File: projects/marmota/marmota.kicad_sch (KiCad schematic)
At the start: 56 parts, among them J1 USB_C, J2 Conn_01x20_Pin, J3 Conn_01x20_Pin, SW1 Button top, SW2 Button side, U1 RP2040, U2 FLASH, U3 MCP73871, U4 RT6160, U5 ESP32, Y1 12MHz

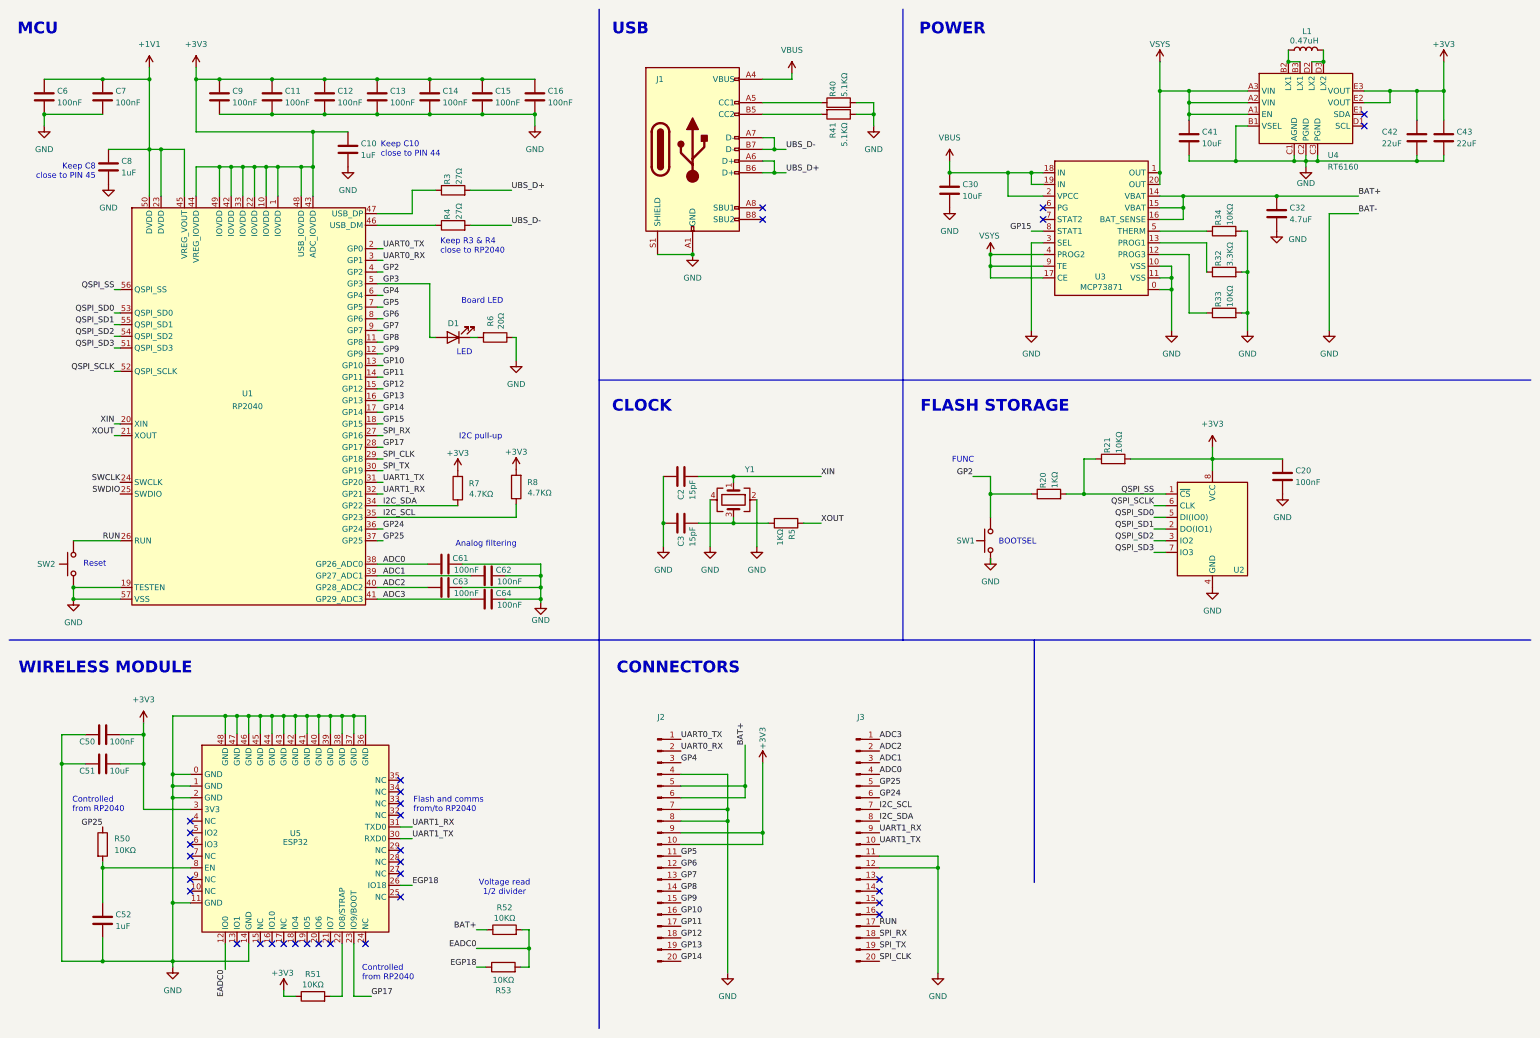
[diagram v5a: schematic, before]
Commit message: Changed power output caps to 47uF in 0603 footprint
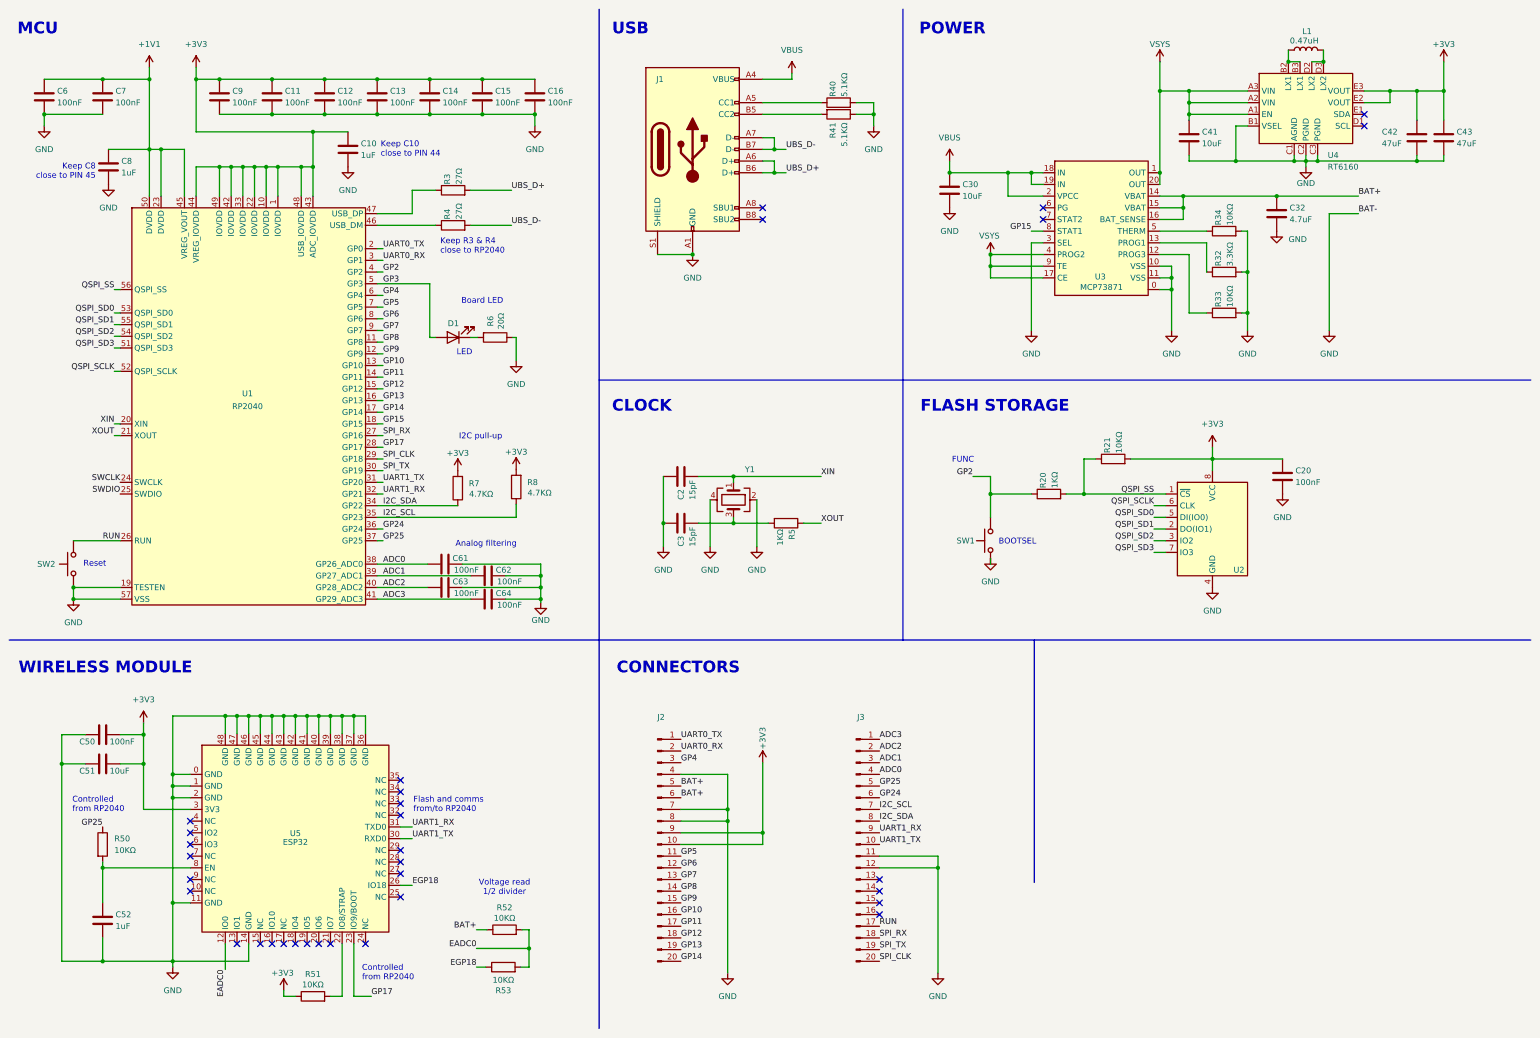
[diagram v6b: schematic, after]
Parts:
- C42, C43: value 22uF -> 47uF; footprint ILO_fp:0402_compact -> ILO_fp:0603_compact; LCSC C105226 -> C730416
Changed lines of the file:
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@@
 	)
 	(junction
-		(at 172.72 181.61)
-		(diameter 0)
-		(color 0 0 0 0)
-	)
-	(junction
 		(at 81.28 27.94)
 		(diameter 0)
@@
 	(wire
 		(pts
-			(xy 172.72 184.15) (xy 172.72 181.61)
-		)
-		(stroke
-			(width 0)
-			(type default)
-		)
-	)
-	(wire
-		(pts
 			(xy 80.01 166.37) (xy 80.01 170.18)
 		)
@@
 	(wire
 		(pts
-			(xy 172.72 181.61) (xy 172.72 172.72)
-		)
-		(stroke
-			(width 0)
-			(type default)
-		)
-	)
-	(wire
-		(pts
 			(xy 93.98 105.41) (xy 92.71 105.41)
 		)
@@
 	(wire
 		(pts
-			(xy 158.75 181.61) (xy 172.72 181.61)
-		)
-		(stroke
-			(width 0)
-			(type default)
-		)
-	)
-	(wire
-		(pts
 			(xy 24.13 176.784) (xy 24.13 219.71)
 		)
@@
 	(wire
 		(pts
-			(xy 158.75 184.15) (xy 172.72 184.15)
-		)
-		(stroke
-			(width 0)
-			(type default)
-		)
-	)
-	(wire
-		(pts
 			(xy 256.54 110.49) (xy 274.32 110.49)
 		)
@@
 		)
 	)
+	(label "BAT+"
+		(at 158.75 184.15 0)
+		(fields_autoplaced yes)
+		(effects
+			(font
+				(size 1.27 1.27)
+			)
+			(justify left bottom)
+		)
+	)
 	(label "ADC2"
 		(at 93.98 138.43 0)
@@
 	)
 	(label "BAT+"
-		(at 172.72 172.72 90)
+		(at 158.75 181.61 0)
 		(fields_autoplaced yes)
 		(effects
@@
 			)
 		)
-		(property "Value" "22uF"
+		(property "Value" "47uF"
 			(at 311.15 41.91 0)
 			(effects
@@
 			)
 		)
-		(property "Footprint" "ILO_fp:0402_compact"
+		(property "Footprint" "ILO_fp:0603_compact"
 			(at 317.8048 36.83 0)
 			(effects
@@
 			)
 		)
-		(property "LCSC" "C105226"
+		(property "LCSC" "C730416"
 			(at 318.77 40.64 0)
 			(effects
@@
 			)
 		)
-		(property "Value" "22uF"
+		(property "Value" "47uF"
 			(at 327.406 41.91 0)
 			(effects
@@
 			)
 		)
-		(property "Footprint" "ILO_fp:0402_compact"
+		(property "Footprint" "ILO_fp:0603_compact"
 			(at 323.6468 36.83 0)
 			(effects
@@
 			)
 		)
-		(property "LCSC" "C105226"
+		(property "LCSC" "C730416"
 			(at 324.612 40.64 0)
 			(effects

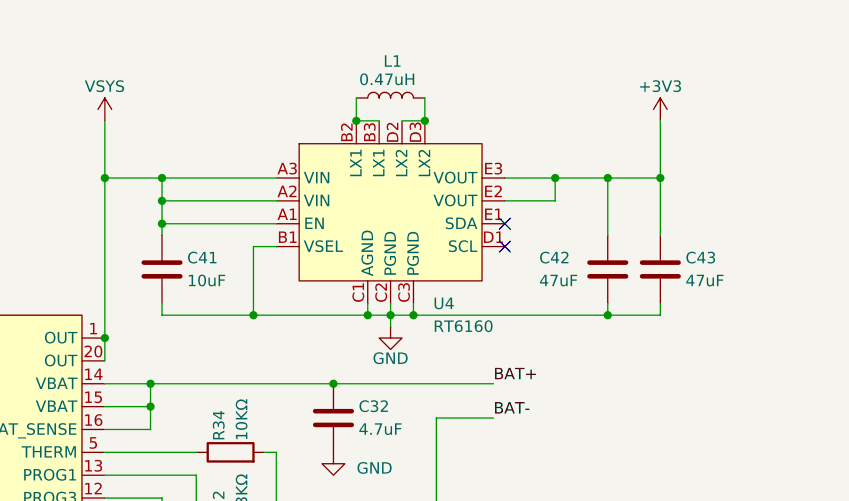
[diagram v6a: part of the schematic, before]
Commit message: Using Richtek 6150 instead of 6160
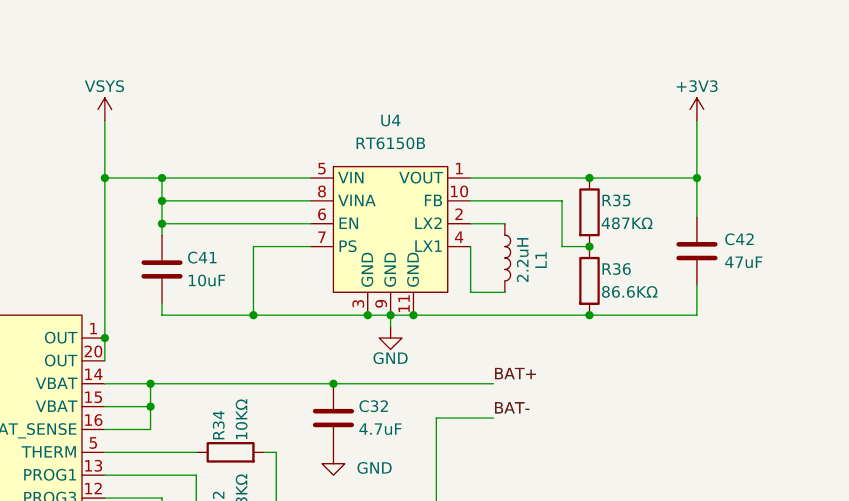
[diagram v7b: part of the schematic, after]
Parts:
- removed C43: 47uF, ILO_fp:0603_compact, symbol Device:C
- removed U4: RT6160, ILO_fp:WL-CSP-15B-1.4x2.3, symbol ILO_sym:Richtek_RT6160
- added R35: 487KΩ, ILO_fp:0402_compact, symbol Device:R
- added R36: 86.6KΩ, ILO_fp:0402_compact, symbol Device:R
- added U4: RT6150B, ILO_fp:WDFN-10L-2.5x2.5, symbol ILO_sym:Richtek_RT6150
- L1: value 0.47uH -> 2.2uH; footprint ILO_fp:SMD_16x10 -> ILO_fp:0603_compact; LCSC C5832340 -> C394950
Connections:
- net +3V3: now also R35.1, U4.1 (VOUT)
- net GND: now also R36.2, U4.11 (GND), U4.3 (GND), U4.7 (PS), U4.9 (GND)
- net VSYS: now also U4.5 (VIN), U4.6 (EN), U4.8 (VINA)
- net at L1.1: now also U4.2 (LX2)
- net at L1.2: now also U4.4 (LX1)
- new net: R35.2, R36.1, U4.10 (FB)
- no-connect marks 33 -> 31
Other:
- moved on the sheet: C42, L1

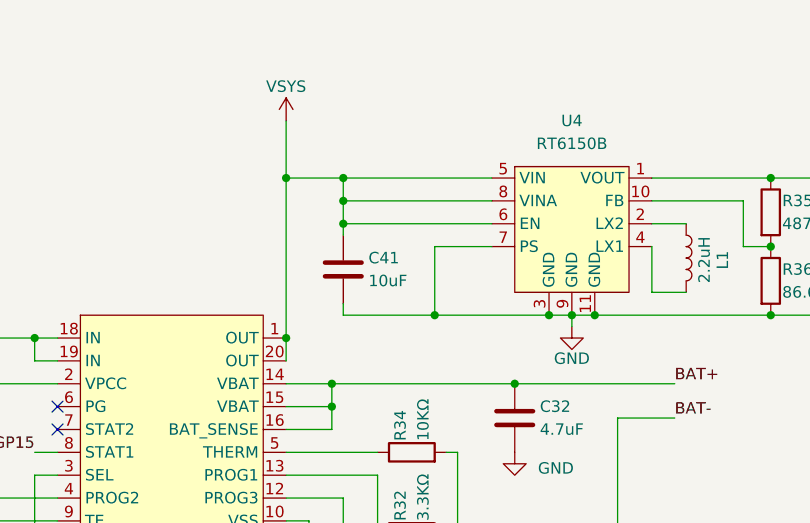
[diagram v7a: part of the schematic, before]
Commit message: Richtek power saving high, Tweaks
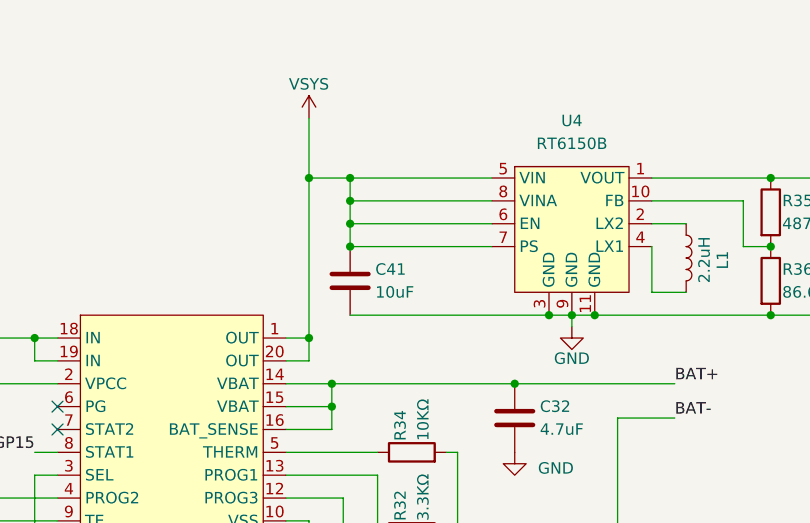
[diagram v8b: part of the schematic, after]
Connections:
- net GND: no longer U4.7 (PS)
- net VSYS: now also U4.7 (PS)
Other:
- moved on the sheet: C41
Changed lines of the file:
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@@
 	)
 	(junction
-		(at 269.24 35.56)
+		(at 270.002 35.56)
 		(diameter 0)
 		(color 0 0 0 0)
@@
 	)
 	(junction
-		(at 269.24 33.02)
+		(at 270.002 33.02)
 		(diameter 0)
 		(color 0 0 0 0)
@@
 	)
 	(junction
-		(at 176.53 191.77)
+		(at 265.43 48.26)
 		(diameter 0)
 		(color 0 0 0 0)
 	)
 	(junction
-		(at 262.89 30.48)
+		(at 176.53 191.77)
 		(diameter 0)
 		(color 0 0 0 0)
@@
 	)
 	(junction
-		(at 279.4 45.72)
-		(diameter 0)
-		(color 0 0 0 0)
-	)
-	(junction
 		(at 78.74 46.99)
 		(diameter 0)
@@
 	)
 	(junction
-		(at 269.24 30.48)
+		(at 270.002 38.1)
+		(diameter 0)
+		(color 0 0 0 0)
+	)
+	(junction
+		(at 270.002 30.48)
 		(diameter 0)
 		(color 0 0 0 0)
@@
 	)
 	(junction
-		(at 262.89 48.26)
-		(diameter 0)
-		(color 0 0 0 0)
-	)
-	(junction
 		(at 297.18 45.72)
 		(diameter 0)
@@
 		(color 0 0 0 0)
 	)
+	(junction
+		(at 265.43 30.48)
+		(diameter 0)
+		(color 0 0 0 0)
+	)
 	(no_connect
 		(at 80.01 215.9)
@@
 	(wire
 		(pts
-			(xy 262.89 48.26) (xy 262.89 50.8)
-		)
-		(stroke
-			(width 0)
-			(type default)
-		)
-	)
-	(wire
-		(pts
 			(xy 45.72 43.18) (xy 45.72 53.34)
 		)
@@
 	(wire
 		(pts
-			(xy 269.24 30.48) (xy 285.75 30.48)
+			(xy 270.002 30.48) (xy 285.75 30.48)
 		)
 		(stroke
@@
 	(wire
 		(pts
-			(xy 269.24 45.72) (xy 279.4 45.72)
-		)
-		(stroke
-			(width 0)
-			(type default)
-		)
-	)
-	(wire
-		(pts
 			(xy 189.23 114.3) (xy 170.18 114.3)
 		)
@@
 	(wire
 		(pts
-			(xy 269.24 35.56) (xy 269.24 36.83)
+			(xy 270.002 35.56) (xy 270.002 38.1)
 		)
 		(stroke
@@
 	(wire
 		(pts
-			(xy 279.4 45.72) (xy 292.1 45.72)
+			(xy 270.002 45.72) (xy 292.1 45.72)
 		)
 		(stroke
@@
 	(wire
 		(pts
-			(xy 262.89 30.48) (xy 269.24 30.48)
+			(xy 265.43 30.48) (xy 270.002 30.48)
 		)
 		(stroke
@@
 	(wire
 		(pts
-			(xy 269.24 30.48) (xy 269.24 33.02)
+			(xy 270.002 30.48) (xy 270.002 33.02)
 		)
 		(stroke
@@
 	(wire
 		(pts
-			(xy 262.89 24.13) (xy 262.89 30.48)
-		)
-		(stroke
-			(width 0)
-			(type default)
-		)
-	)
-	(wire
-		(pts
 			(xy 226.06 71.12) (xy 237.49 71.12)
 		)
@@
 	(wire
 		(pts
-			(xy 279.4 38.1) (xy 285.75 38.1)
-		)
-		(stroke
-			(width 0)
-			(type default)
-		)
-	)
-	(wire
-		(pts
 			(xy 175.26 119.38) (xy 175.26 129.54)
 		)
@@
 	(wire
 		(pts
-			(xy 262.89 30.48) (xy 262.89 48.26)
+			(xy 265.43 23.876) (xy 265.43 30.48)
 		)
 		(stroke
@@
 	(wire
 		(pts
+			(xy 265.43 48.26) (xy 262.89 48.26)
+		)
+		(stroke
+			(width 0)
+			(type default)
+		)
+	)
+	(wire
+		(pts
 			(xy 288.29 53.34) (xy 306.07 53.34)
 		)
@@
 	(wire
 		(pts
-			(xy 269.24 33.02) (xy 269.24 35.56)
+			(xy 270.002 33.02) (xy 270.002 35.56)
 		)
 		(stroke
@@
 	(wire
 		(pts
-			(xy 269.24 33.02) (xy 285.75 33.02)
+			(xy 270.002 33.02) (xy 285.75 33.02)
 		)
 		(stroke
@@
 	(wire
 		(pts
-			(xy 269.24 45.72) (xy 269.24 44.45)
+			(xy 189.23 33.02) (xy 176.53 33.02)
 		)
 		(stroke
@@
 	(wire
 		(pts
-			(xy 189.23 33.02) (xy 176.53 33.02)
+			(xy 234.95 48.26) (xy 237.49 48.26)
 		)
 		(stroke
@@
 	(wire
 		(pts
-			(xy 234.95 48.26) (xy 237.49 48.26)
+			(xy 92.71 123.19) (xy 122.936 123.19)
 		)
 		(stroke
@@
 	(wire
 		(pts
-			(xy 92.71 123.19) (xy 122.936 123.19)
+			(xy 265.43 50.8) (xy 265.43 48.26)
 		)
 		(stroke
@@
 	(wire
 		(pts
-			(xy 269.24 35.56) (xy 285.75 35.56)
+			(xy 270.002 35.56) (xy 285.75 35.56)
 		)
 		(stroke
@@
 	(wire
 		(pts
+			(xy 262.89 50.8) (xy 265.43 50.8)
+		)
+		(stroke
+			(width 0)
+			(type default)
+		)
+	)
+	(wire
+		(pts
 			(xy 262.89 71.12) (xy 265.43 71.12)
 		)
@@
 	(wire
 		(pts
+			(xy 270.002 38.1) (xy 285.75 38.1)
+		)
+		(stroke
+			(width 0)
+			(type default)
+		)
+	)
+	(wire
+		(pts
 			(xy 41.91 167.894) (xy 41.91 170.434)
 		)
@@
 	(wire
 		(pts
-			(xy 201.93 199.39) (xy 214.63 199.39)
+			(xy 265.43 30.48) (xy 265.43 48.26)
 		)
 		(stroke
@@
 	(wire
 		(pts
-			(xy 313.69 38.1) (xy 316.738 38.1)
+			(xy 201.93 199.39) (xy 214.63 199.39)
 		)
 		(stroke
@@
 	(wire
 		(pts
-			(xy 179.07 43.18) (xy 181.61 43.18)
+			(xy 313.69 38.1) (xy 316.738 38.1)
 		)
 		(stroke
@@
 	(wire
 		(pts
-			(xy 274.32 110.49) (xy 289.56 110.49)
+			(xy 179.07 43.18) (xy 181.61 43.18)
 		)
 		(stroke
@@
 	(wire
 		(pts
-			(xy 214.63 199.39) (xy 214.63 222.25)
+			(xy 274.32 110.49) (xy 289.56 110.49)
 		)
 		(stroke
@@
 	(wire
 		(pts
-			(xy 279.4 38.1) (xy 279.4 45.72)
+			(xy 214.63 199.39) (xy 214.63 222.25)
 		)
 		(stroke
@@
 	(symbol
 		(lib_id "Device:C")
-		(at 269.24 40.64 180)
+		(at 270.002 41.91 180)
 		(unit 1)
 		(exclude_from_sim no)
@@
 		(dnp no)
 		(property "Reference" "C41"
-			(at 272.034 39.37 0)
+			(at 272.796 40.64 0)
 			(effects
 				(font
@@
 		)
 		(property "Value" "10uF"
-			(at 272.034 41.91 0)
+			(at 272.796 43.18 0)
 			(effects
 				(font
@@
 		)
 		(property "Footprint" "ILO_fp:0402_compact"
-			(at 268.2748 36.83 0)
+			(at 269.0368 38.1 0)
 			(effects
 				(font
@@
 		)
 		(property "Datasheet" "~"
-			(at 269.24 40.64 0)
+			(at 270.002 41.91 0)
 			(effects
 				(font
@@
 		)
 		(property "Description" "Unpolarized capacitor"
-			(at 269.24 40.64 0)
+			(at 270.002 41.91 0)
 			(effects
 				(font
@@
 		)
 		(property "LCSC" "C15525"
-			(at 269.24 40.64 0)
+			(at 270.002 41.91 0)
 			(effects
 				(font
@@
 		)
 		(property "Export" "yes"
-			(at 269.24 40.64 0)
+			(at 270.002 41.91 0)
 			(effects
 				(font
@@
 		)
 		(property "Group" "C"
-			(at 269.24 40.64 0)
+			(at 270.002 41.91 0)
 			(effects
 				(font
@@
 		)
 		(property "Mount" "SMD"
-			(at 269.24 40.64 0)
+			(at 270.002 41.91 0)
 			(effects
 				(font
@@
 	(symbol
 		(lib_id "power:+3V3")
-		(at 262.89 24.13 0)
+		(at 265.43 23.876 0)
 		(unit 1)
 		(exclude_from_sim no)
@@
 		(dnp no)
 		(property "Reference" "#PWR037"
-			(at 262.89 27.94 0)
+			(at 265.43 27.686 0)
 			(effects
 				(font
@@
 		)
 		(property "Value" "VSYS"
-			(at 262.89 20.32 0)
+			(at 265.43 20.066 0)
 			(effects
 				(font
@@
 		)
 		(property "Footprint" ""
-			(at 262.89 24.13 0)
+			(at 265.43 23.876 0)
 			(effects
 				(font
@@
 		)
 		(property "Datasheet" ""
-			(at 262.89 24.13 0)
+			(at 265.43 23.876 0)
 			(effects
 				(font
@@
 		)
 		(property "Description" "Power symbol creates a global label with name \"+3V3\""
-			(at 262.89 24.13 0)
+			(at 265.43 23.876 0)
 			(effects
 				(font
